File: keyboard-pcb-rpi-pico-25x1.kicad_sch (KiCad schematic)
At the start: 31 parts, among them SW1 SW_Push, SW10 SW_Push, SW11 SW_Push, SW12 SW_Push, SW13 SW_Push, SW14 SW_Push, SW15 SW_Push, SW16 SW_Push, SW17 SW_Push, SW18 SW_Push, SW19 SW_Push, SW2 SW_Push, SW20 SW_Push, SW21 SW_Push, SW22 SW_Push, SW23 SW_Push, SW24 SW_Push, SW25 SW_Push, SW3 SW_Push, SW4 SW_Push, SW5 SW_Push, SW6 SW_Push, SW7 SW_Push, SW8 SW_Push, SW9 SW_Push

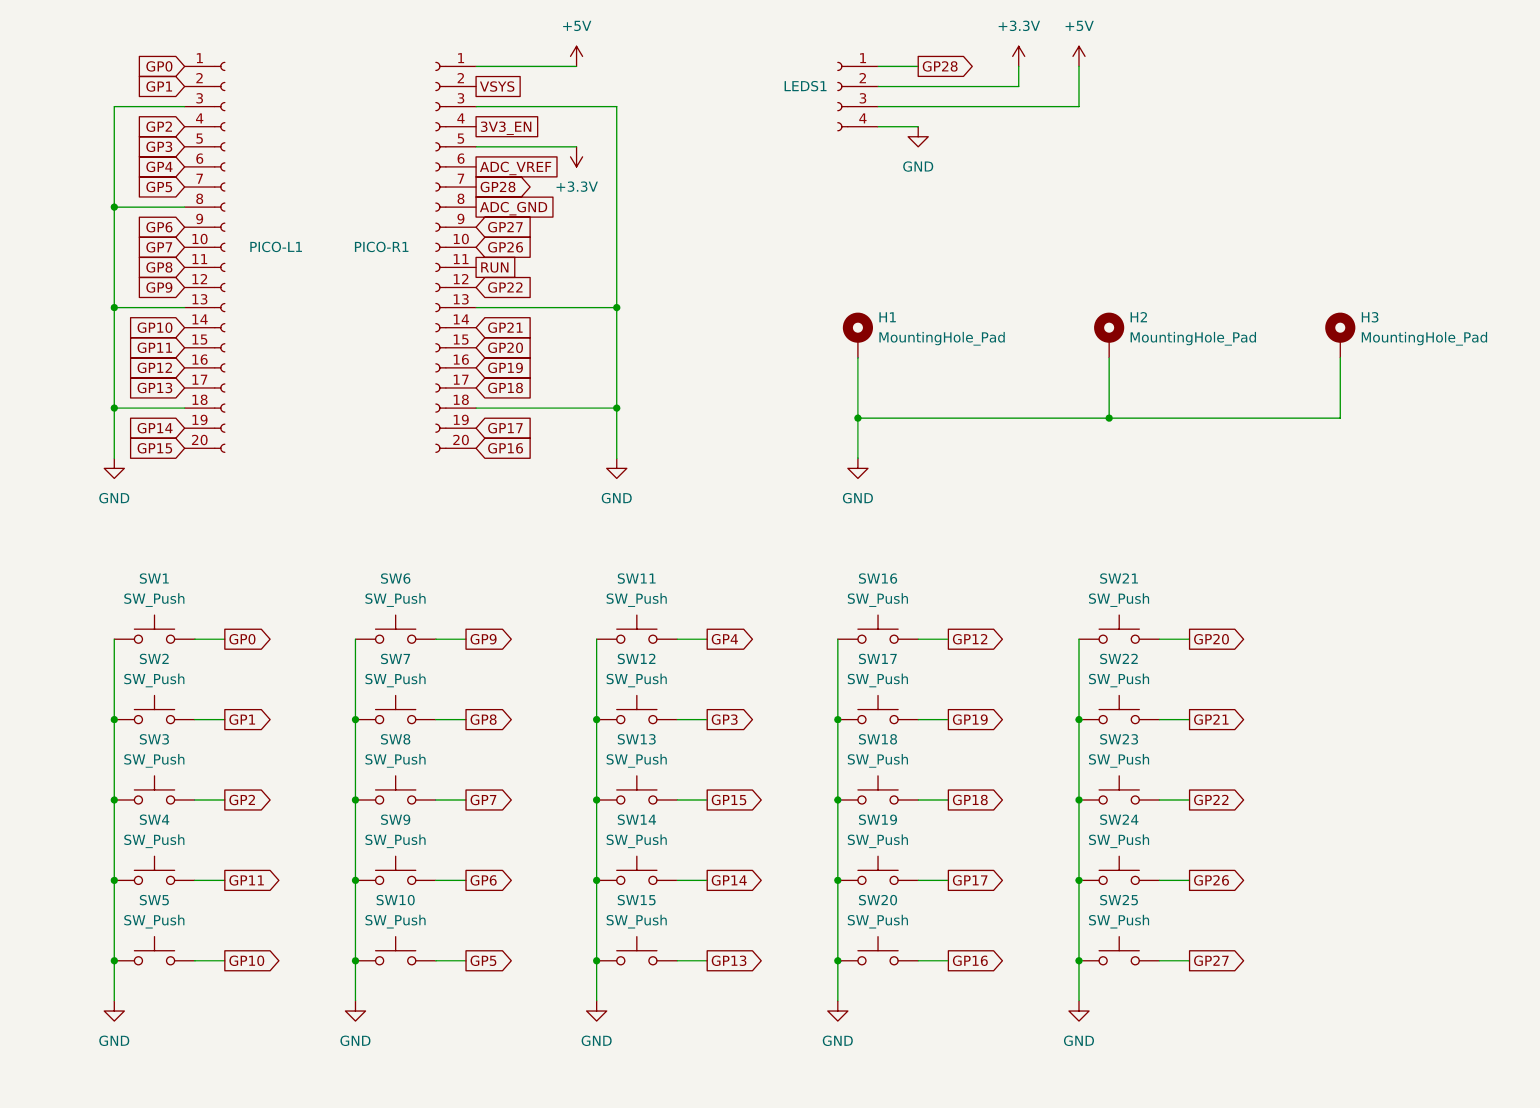
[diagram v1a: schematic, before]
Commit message: Move the ground to the other side of the switch pins
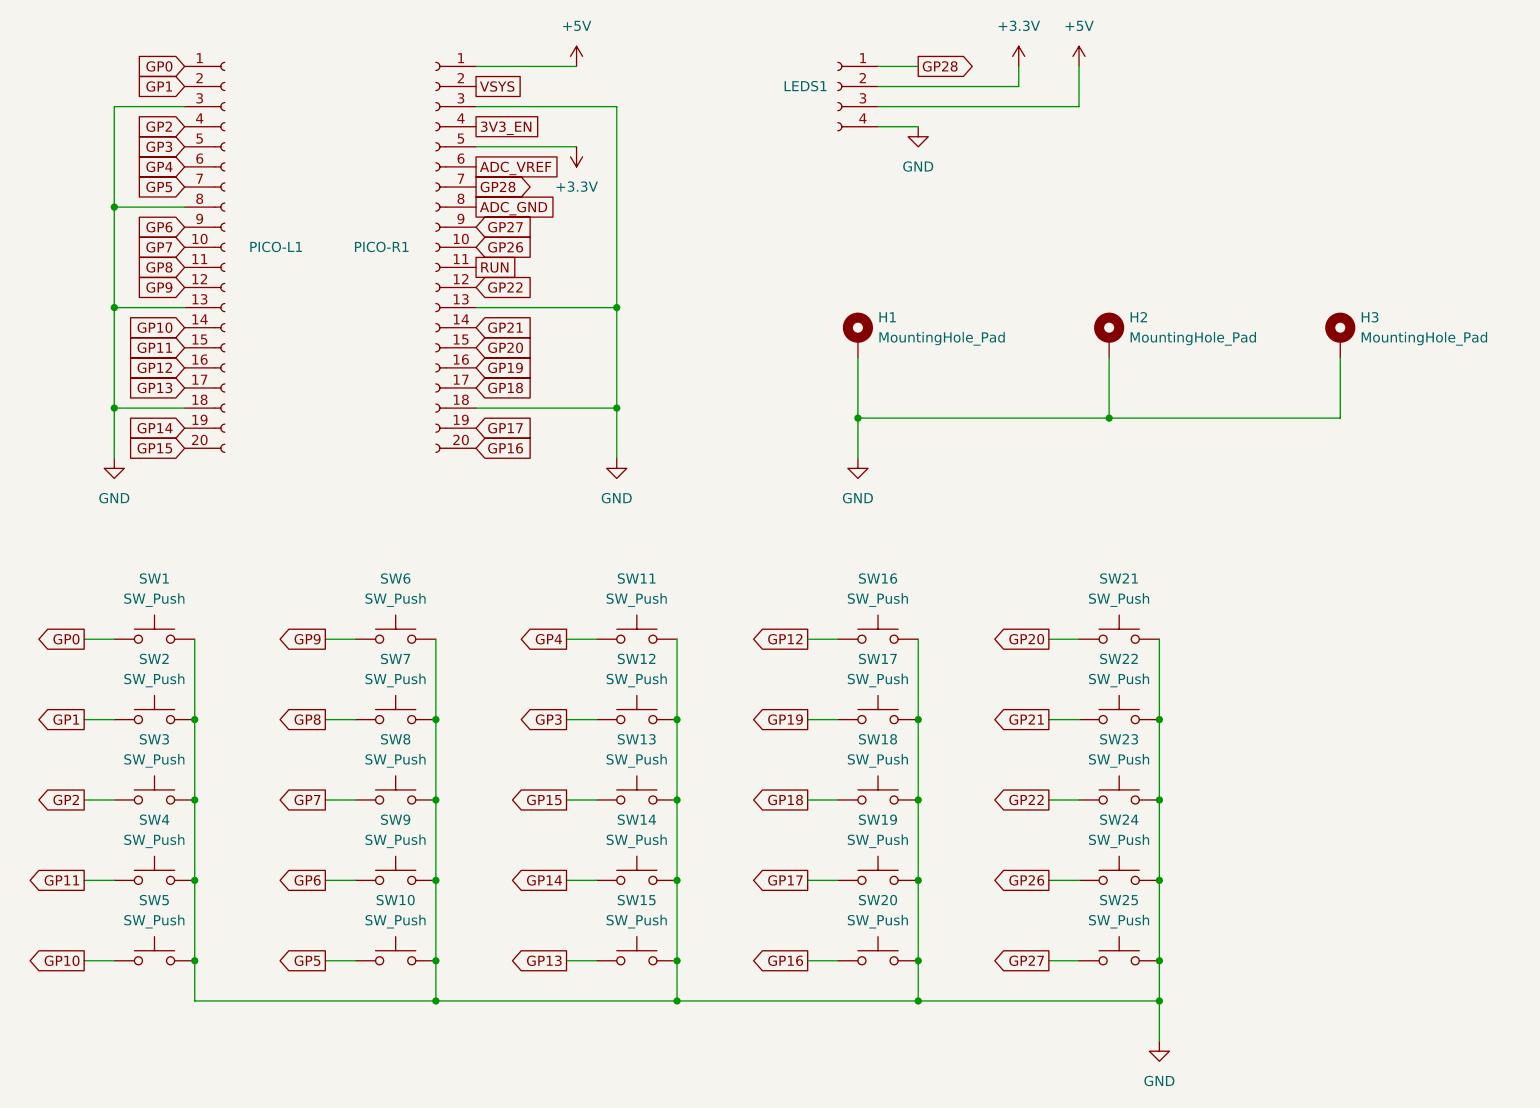
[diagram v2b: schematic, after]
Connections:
- net GND: now also SW1.2, SW10.2, SW11.2, SW12.2, SW13.2, SW14.2, SW15.2, SW16.2, SW17.2, SW18.2, SW19.2, SW2.2, SW20.2, SW21.2, SW22.2, SW23.2, SW24.2, SW25.2, SW3.2, SW4.2, SW5.2, SW6.2, SW7.2, SW8.2, SW9.2; no longer SW1.1, SW10.1, SW11.1, SW12.1, SW13.1, SW14.1, SW15.1, SW16.1, SW17.1, SW18.1, SW19.1, SW2.1, SW20.1, SW21.1, SW22.1, SW23.1, SW24.1, SW25.1, SW3.1, SW4.1, SW5.1, SW6.1, SW7.1, SW8.1, SW9.1
- net GP0: now also SW1.1; no longer SW1.2
- net GP1: now also SW2.1; no longer SW2.2
- net GP10: now also SW5.1; no longer SW5.2
- net GP11: now also SW4.1; no longer SW4.2
- net GP12: now also SW16.1; no longer SW16.2
- net GP13: now also SW15.1; no longer SW15.2
- net GP14: now also SW14.1; no longer SW14.2
- net GP15: now also SW13.1; no longer SW13.2
- net GP16: now also SW20.1; no longer SW20.2
- net GP17: now also SW19.1; no longer SW19.2
- net GP18: now also SW18.1; no longer SW18.2
- net GP19: now also SW17.1; no longer SW17.2
- net GP2: now also SW3.1; no longer SW3.2
- net GP20: now also SW21.1; no longer SW21.2
- net GP21: now also SW22.1; no longer SW22.2
- net GP22: now also SW23.1; no longer SW23.2
- net GP26: now also SW24.1; no longer SW24.2
- net GP27: now also SW25.1; no longer SW25.2
- net GP3: now also SW12.1; no longer SW12.2
- net GP4: now also SW11.1; no longer SW11.2
- net GP5: now also SW10.1; no longer SW10.2
- net GP6: now also SW9.1; no longer SW9.2
- net GP7: now also SW8.1; no longer SW8.2
- net GP8: now also SW7.1; no longer SW7.2
- net GP9: now also SW6.1; no longer SW6.2

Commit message: Fix schematic power error messages by adding PWR_FLAG
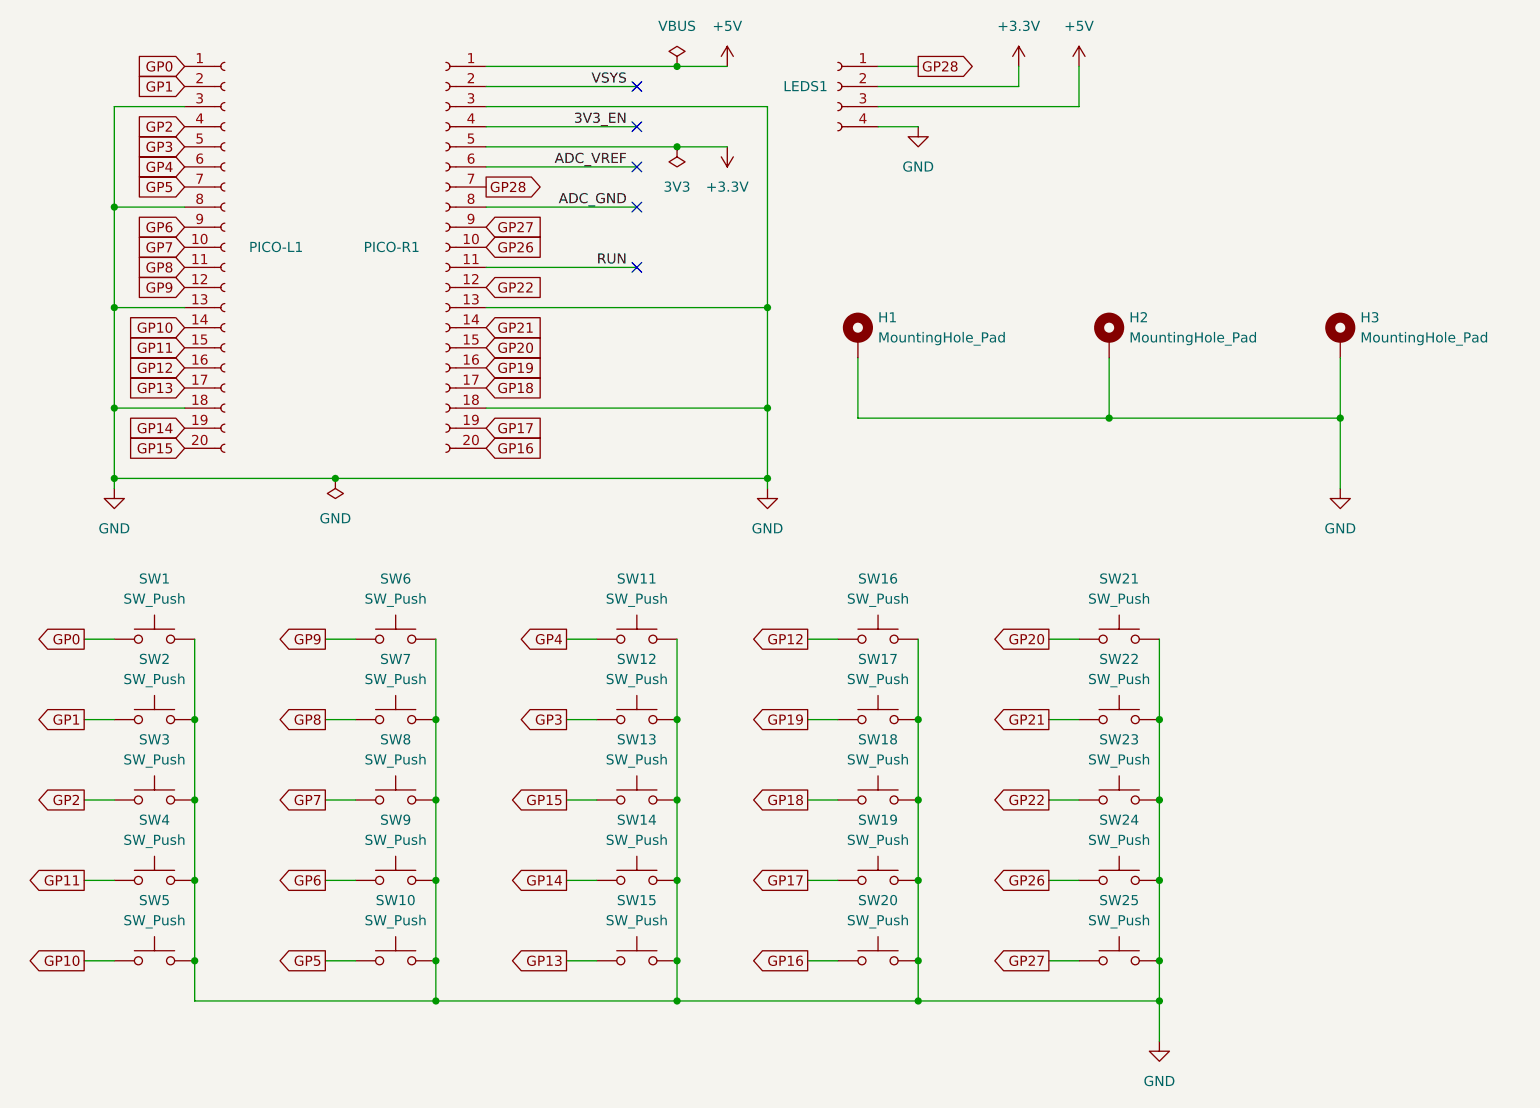
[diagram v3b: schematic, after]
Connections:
- no-connect marks 0 -> 5
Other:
- moved on the sheet: PICO-R1
